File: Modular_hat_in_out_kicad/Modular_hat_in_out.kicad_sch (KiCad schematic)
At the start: 60 parts, among them J1 Raspberry_Pi_2_3, U1 MCP3008, U2 LM324, U3 MCP3008, U4 MCP4728, U5 MCP4728, U6 LM324

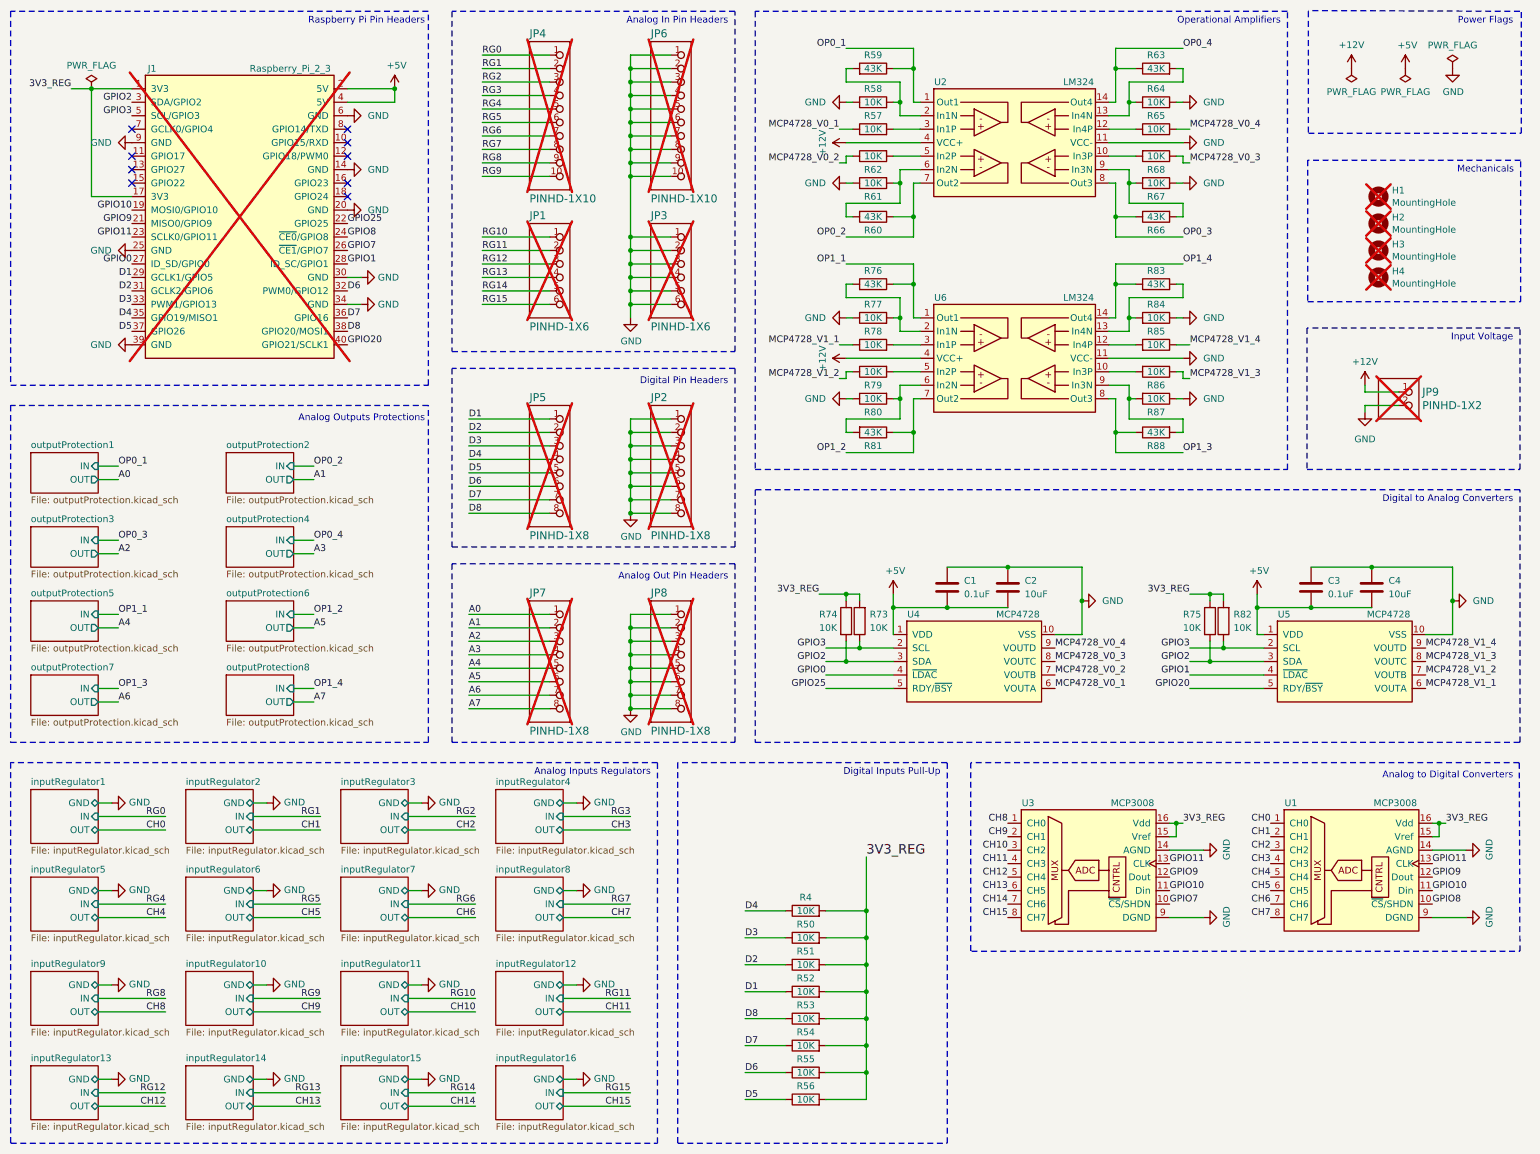
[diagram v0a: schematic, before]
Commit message: [ADD] 5V Input voltage in schematics + clean
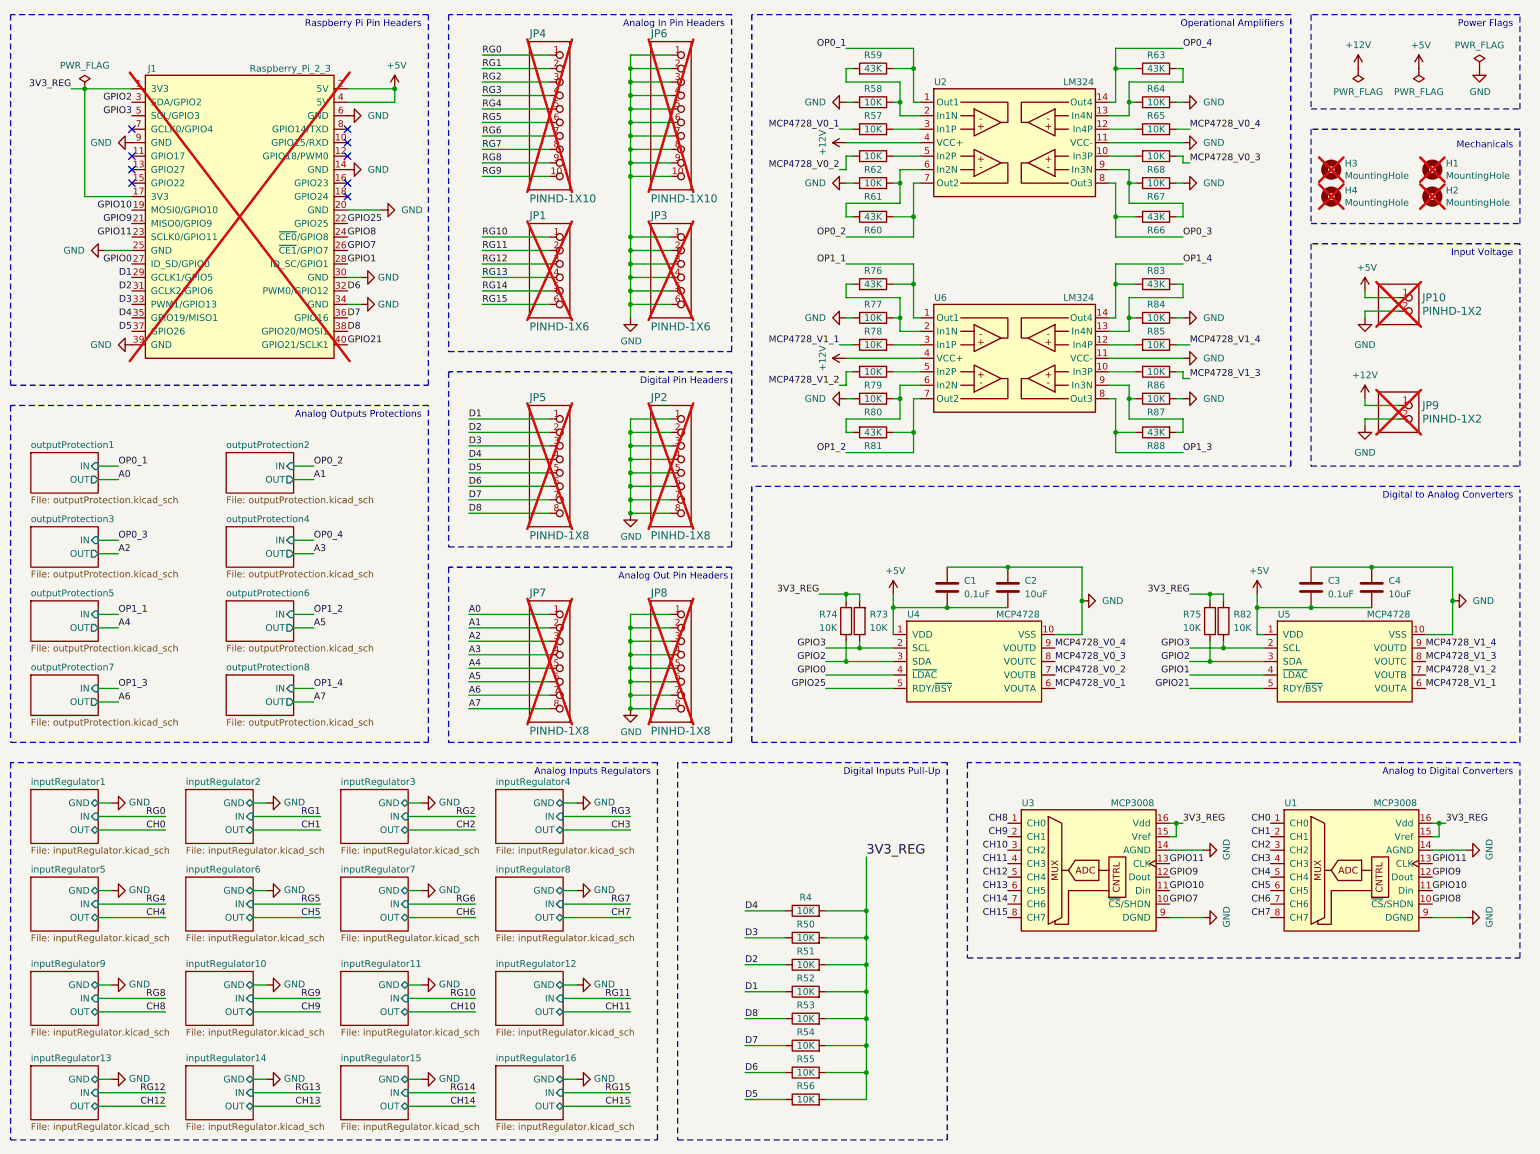
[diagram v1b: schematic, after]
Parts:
- added JP10: PINHD-1X2, Modular Shield:1X02-BIG, symbol Modular Shield:PINHD-1X2
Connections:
- net +5V: now also JP10.1
- net GND: now also JP10.2
- net GPIO20 renamed GPIO21
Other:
- moved on the sheet: H1, H2, H3, H4, JP9

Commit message: [ADD] New Revision 1.1
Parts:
- U1, U3: JLCPCB Position Offset 0, -0.16 -> (none); JLCPCB Rotation Offset 270 -> (none); Position Offset (none) -> 0, -0.0; Rotation Offset (none) -> 270
- U2, U6: JLCPCB Rotation Offset 270 -> (none); Rotation Offset (none) -> 270
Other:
- title: Modular Hat -> Pigeons
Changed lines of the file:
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@@
 	(paper "User" 317.627 242.138)
 	(title_block
-		(title "Modular Hat")
-		(date "2024-08-21")
-		(rev "1.0")
+		(title "Pigeons")
+		(date "2025-10-28")
+		(rev "1.1")
 	)
 	(text "Analog Outputs Protections"
@@
 			)
 		)
-		(property "JLCPCB Rotation Offset" "270"
+		(property "Position Offset" "0, -0.0"
 			(at 269.24 175.26 0)
 			(effects
@@
 			)
 		)
-		(property "JLCPCB Position Offset" "0, -0.16"
+		(property "Rotation Offset" "270"
 			(at 269.24 175.26 0)
 			(effects
@@
 			)
 		)
-		(property "JLCPCB Rotation Offset" "270"
+		(property "Position Offset" "0, -0.0"
 			(at 219.71 175.26 0)
 			(effects
@@
 			)
 		)
-		(property "JLCPCB Position Offset" "0, -0.16"
+		(property "Rotation Offset" "270"
 			(at 219.71 175.26 0)
 			(effects
@@
 			)
 		)
-		(property "JLCPCB Rotation Offset" "270"
+		(property "Rotation Offset" "270"
 			(at 205.74 76.2 0)
 			(effects
@@
 			)
 		)
-		(property "JLCPCB Rotation Offset" "270"
+		(property "Rotation Offset" "270"
 			(at 205.74 35.56 0)
 			(effects
